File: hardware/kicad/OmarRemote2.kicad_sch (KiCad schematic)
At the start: 13 parts, among them SW1 SW_Push, SW2 SW_Push, SW3 SW_Push, SW4 SW_Push, SW5 SW_Push, SW6 SW_Push, U1 XIAO-ESP32-S3-SMD

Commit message: feat: add IR-Sender
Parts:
- added IR1: KY-005, symbol KY-005_IR:KY-005_IR_Sender
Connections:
- net 5V: now also IR1.2 (Vcc)
- net GND: now also IR1.3 (GND)
- net IR: now also IR1.1 (INPUT)
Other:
- note added: "IR-Sender"
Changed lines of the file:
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@@
+	)
+	(rectangle
+		(start 127 97.79)
+		(end 162.56 124.46)
+		(stroke
+			(width 0)
+			(type default)
+		)
+		(fill
+			(type none)
+		)
 	)
 	(rectangle
@@
 		(exclude_from_sim no)
 		(at 239.014 34.544 0)
+		(effects
+			(font
+				(size 1.27 1.27)
+			)
+		)
+	)
+	(text "IR-Sender"
+		(exclude_from_sim no)
+		(at 131.826 96.774 0)
 		(effects
 			(font
@@
 	(wire
 		(pts
+			(xy 160.02 106.68) (xy 160.02 116.84)
+		)
+		(stroke
+			(width 0)
+			(type default)
+		)
+	)
+	(wire
+		(pts
 			(xy 116.84 48.26) (xy 121.92 48.26)
 		)
@@
 	(wire
 		(pts
+			(xy 144.78 106.68) (xy 160.02 106.68)
+		)
+		(stroke
+			(width 0)
+			(type default)
+		)
+	)
+	(wire
+		(pts
 			(xy 57.15 50.8) (xy 57.15 66.04)
 		)
@@
 	(wire
 		(pts
+			(xy 144.78 114.3) (xy 151.13 114.3)
+		)
+		(stroke
+			(width 0)
+			(type default)
+		)
+	)
+	(wire
+		(pts
 			(xy 57.15 111.76) (xy 57.15 121.92)
 		)
@@
 	(wire
 		(pts
+			(xy 144.78 110.49) (xy 151.13 110.49)
+		)
+		(stroke
+			(width 0)
+			(type default)
+		)
+	)
+	(wire
+		(pts
 			(xy 140.97 73.66) (xy 140.97 76.2)
 		)
@@
 		)
 	)
+	(global_label "IR"
+		(shape input)
+		(at 151.13 114.3 0)
+		(fields_autoplaced yes)
+		(effects
+			(font
+				(size 1.27 1.27)
+			)
+			(justify left)
+		)
+		(property "Intersheetrefs" "${INTERSHEET_REFS}"
+			(at 155.99 114.3 0)
+			(effects
+				(font
+					(size 1.27 1.27)
+				)
+				(justify left)
+				(hide yes)
+			)
+		)
+	)
 	(global_label "ButtonBACK"
 		(shape input)
@@
 				)
 				(justify right)
+				(hide yes)
+			)
+		)
+	)
+	(global_label "5V"
+		(shape input)
+		(at 151.13 110.49 0)
+		(fields_autoplaced yes)
+		(effects
+			(font
+				(size 1.27 1.27)
+			)
+			(justify left)
+		)
+		(property "Intersheetrefs" "${INTERSHEET_REFS}"
+			(at 156.4133 110.49 0)
+			(effects
+				(font
+					(size 1.27 1.27)
+				)
+				(justify left)
 				(hide yes)
 			)
@@
 	)
 	(symbol
+		(lib_id "KY-005_IR:KY-005_IR_Sender")
+		(at 129.54 105.41 0)
+		(unit 1)
+		(exclude_from_sim no)
+		(in_bom yes)
+		(on_board yes)
+		(dnp no)
+		(fields_autoplaced yes)
+		(property "Reference" "IR1"
+			(at 135.89 100.33 0)
+			(effects
+				(font
+					(size 1.27 1.27)
+				)
+			)
+		)
+		(property "Value" "KY-005"
+			(at 135.89 102.87 0)
+			(effects
+				(font
+					(size 1.27 1.27)
+				)
+			)
+		)
+		(property "Footprint" ""
+			(at 129.54 105.41 0)
+			(effects
+				(font
+					(size 1.27 1.27)
+				)
+				(hide yes)
+			)
+		)
+		(property "Datasheet" ""
+			(at 129.54 105.41 0)
+			(effects
+				(font
+					(size 1.27 1.27)
+				)
+				(hide yes)
+			)
+		)
+		(property "Description" ""
+			(at 129.54 105.41 0)
+			(effects
+				(font
+					(size 1.27 1.27)
+				)
+				(hide yes)
+			)
+		)
+		(pin "1"
+		)
+		(pin "2"
+		)
+		(pin "3"
+		)
+		(instances
+			(project ""
+				(path "/1bf0dd3a-ef06-4d9e-bc1a-d833f6081a87"
+					(reference "IR1")
+					(unit 1)
+				)
+			)
+		)
+	)
+	(symbol
 		(lib_id "Device:R")
 		(at 259.08 130.81 90)
@@
 					(unit 1)
 				)
+			)
+		)
+	)
+	(symbol
+		(lib_id "power:GND")
+		(at 160.02 116.84 0)
+		(unit 1)
+		(exclude_from_sim no)
+		(in_bom yes)
+		(on_board yes)
+		(dnp no)
+		(fields_autoplaced yes)
+		(property "Reference" "#PWR02"
+			(at 160.02 123.19 0)
+			(effects
+				(font
+					(size 1.27 1.27)
+				)
+				(hide yes)
+			)
+		)
+		(property "Value" "GND"
+			(at 160.02 121.92 0)
+			(effects
+				(font
+					(size 1.27 1.27)
+				)
+			)
+		)
+		(property "Footprint" ""
+			(at 160.02 116.84 0)
+			(effects
+				(font
+					(size 1.27 1.27)
+				)
+				(hide yes)
+			)
+		)
+		(property "Datasheet" ""
+			(at 160.02 116.84 0)
+			(effects
+				(font
+					(size 1.27 1.27)
+				)
+				(hide yes)
+			)
+		)
+		(property "Description" "Power symbol creates a global label with name \"GND\" , ground"
+			(at 160.02 116.84 0)
+			(effects
+				(font
+					(size 1.27 1.27)
+				)
+				(hide yes)
+			)
+		)
+		(pin "1"
+		)
+		(instances
+			(project ""
+				(path "/1bf0dd3a-ef06-4d9e-bc1a-d833f6081a87"
+					(reference "#PWR02")
+					(unit 1)
+				)

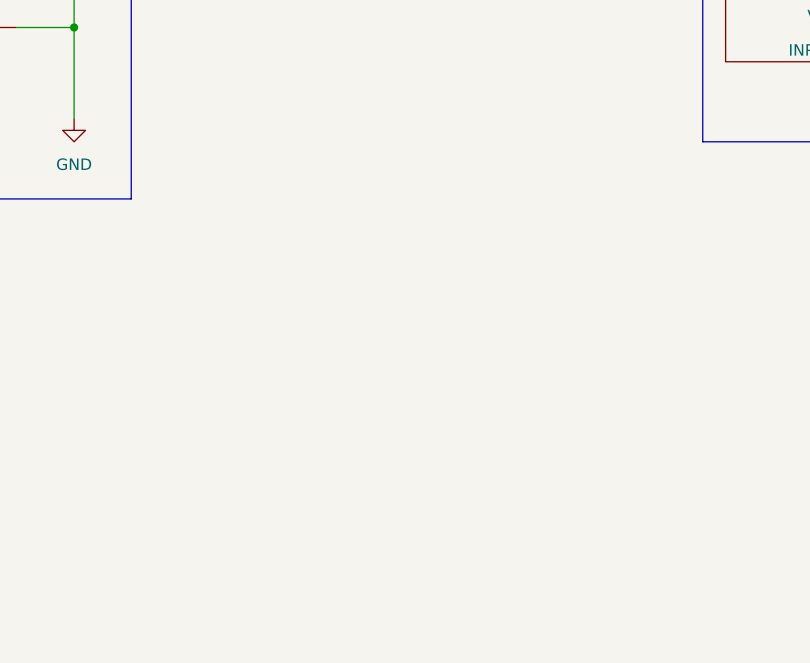
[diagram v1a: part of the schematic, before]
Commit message: feat: add battery charger to schematic
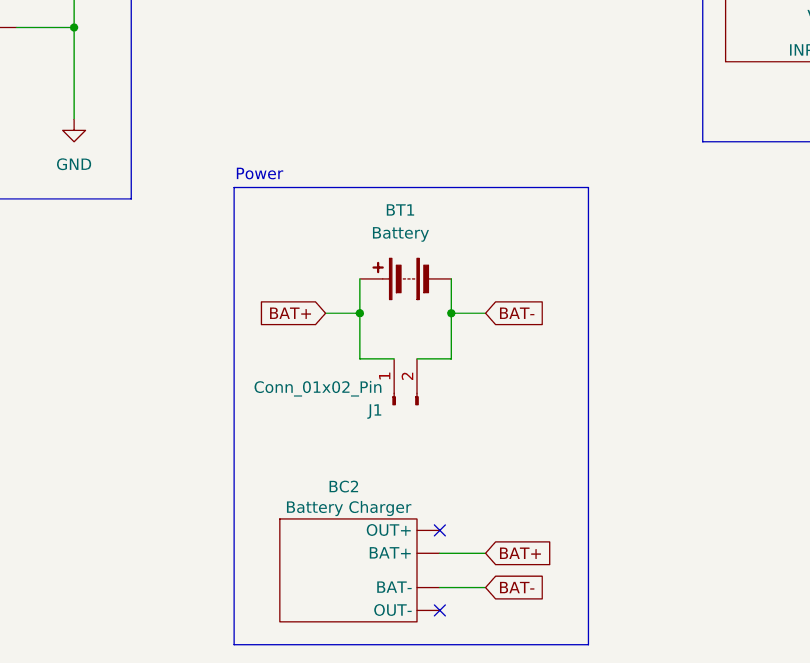
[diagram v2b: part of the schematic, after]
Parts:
- added BC2: Battery Charger, symbol TP4056_USB-C_Protect_Module:TP4056_USB-C_Protect_Module
- added BT1: Battery, Battery:BatteryHolder_Keystone_1042_1x18650, symbol Device:Battery
- added J1: Conn_01x02_Pin, symbol Connector:Conn_01x02_Pin
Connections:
- net BAT+: now also BC2. (OUT-), BT1.1 (+), J1.1 (Pin_1)
- net BAT-: now also BC2. (OUT-), BT1.2 (-), J1.2 (Pin_2)
- no-connect marks 0 -> 2
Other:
- note added: "Power"
